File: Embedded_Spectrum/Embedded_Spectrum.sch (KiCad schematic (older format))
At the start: 20 parts, among them J1 USB_OTG, J2 AudioJack2, U1 LM1117-ADJ, U2 STM32F411RETx

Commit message: Added jack
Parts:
- removed J2: AudioJack2, symbol Connector:AudioJack2
- added C?: 100 nF, symbol Device:C
- added J2: AudioJack2_Ground, symbol Connector:AudioJack2_Ground
- added R? (x2): 10k, symbol Device:R
- added R?: 1k, symbol Device:R
- R1: value 100 -> 1000
- R2: value 220 -> 2200
- R3: value 180 -> 1800
- R4: value 820 -> 8200
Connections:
- net +3V3: now also R?.1
- net GND: now also J2.G, R?.2
- net J_IN: now reaches U2.14 (PA0)
- net J_IN: now also R?.1
- new net: C?.2, J2.S, J2.T
- new net: C?.1, R?.1, R?.2, R?.2
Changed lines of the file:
@@
 EESchema Schematic File Version 4
+LIBS:Embedded_Spectrum-cache
 EELAYER 26 0
 EELAYER END
@@
 P 4000 950
 F 0 "R1" H 4070 996 50  0000 L CNN
-F 1 "100" H 4070 905 50  0000 L CNN
+F 1 "1000" H 4070 905 50  0000 L CNN
 F 2 "" V 3930 950 50  0001 C CNN
 F 3 "~" H 4000 950 50  0001 C CNN
@@
 P 4000 1250
 F 0 "R2" H 4070 1296 50  0000 L CNN
-F 1 "220" H 4070 1205 50  0000 L CNN
+F 1 "2200" H 4070 1205 50  0000 L CNN
 F 2 "" V 3930 1250 50  0001 C CNN
 F 3 "~" H 4000 1250 50  0001 C CNN
@@
 P 4000 1550
 F 0 "R3" H 4070 1596 50  0000 L CNN
-F 1 "180" H 4070 1505 50  0000 L CNN
+F 1 "1800" H 4070 1505 50  0000 L CNN
 F 2 "" V 3930 1550 50  0001 C CNN
 F 3 "~" H 4000 1550 50  0001 C CNN
@@
 P 4000 1900
 F 0 "R4" H 4070 1946 50  0000 L CNN
-F 1 "820" H 4070 1855 50  0000 L CNN
+F 1 "8200" H 4070 1855 50  0000 L CNN
 F 2 "" V 3930 1900 50  0001 C CNN
 F 3 "~" H 4000 1900 50  0001 C CNN
@@
 $EndComp
 $Comp
-L Connector:AudioJack2 J2
-U 1 1 5C5D57A2
-P 6250 1350
-F 0 "J2" H 6280 1675 50  0000 C CNN
-F 1 "AudioJack2" H 6280 1584 50  0000 C CNN
-F 2 "" H 6250 1350 50  0001 C CNN
-F 3 "~" H 6250 1350 50  0001 C CNN
-	1    6250 1350
-	1    0    0    -1
-$EndComp
+L Connector:AudioJack2_Ground J2
+U 1 1 5C5D0CF5
+P 1500 4400
+F 0 "J2" H 1530 4725 50  0000 C CNN
+F 1 "AudioJack2_Ground" H 1530 4634 50  0000 C CNN
+F 2 "" H 1500 4400 50  0001 C CNN
+F 3 "~" H 1500 4400 50  0001 C CNN
+	1    1500 4400
+	1    0    0    -1
+$EndComp
+$Comp
+L power:GND #PWR?
+U 1 1 5C5C6E39
+P 1500 4600
+F 0 "#PWR?" H 1500 4350 50  0001 C CNN
+F 1 "GND" H 1505 4427 50  0000 C CNN
+F 2 "" H 1500 4600 50  0001 C CNN
+F 3 "" H 1500 4600 50  0001 C CNN
+	1    1500 4600
+	1    0    0    -1
+$EndComp
+Wire Wire Line
+	1700 4400 1850 4400
+Wire Wire Line
+	1700 4300 1850 4300
+Wire Wire Line
+	1850 4300 1850 4400
+Connection ~ 1850 4400
+Wire Wire Line
+	1850 4400 1950 4400
+$Comp
+L Device:C C?
+U 1 1 5C6539D7
+P 2100 4400
+F 0 "C?" V 1848 4400 50  0000 C CNN
+F 1 "100 nF" V 1939 4400 50  0000 C CNN
+F 2 "" H 2138 4250 50  0001 C CNN
+F 3 "~" H 2100 4400 50  0001 C CNN
+	1    2100 4400
+	0    1    1    0
+$EndComp
+Wire Wire Line
+	2250 4400 2350 4400
+$Comp
+L Device:R R?
+U 1 1 5C6577EA
+P 2350 4250
+F 0 "R?" H 2420 4296 50  0000 L CNN
+F 1 "10k" H 2420 4205 50  0000 L CNN
+F 2 "" V 2280 4250 50  0001 C CNN
+F 3 "~" H 2350 4250 50  0001 C CNN
+	1    2350 4250
+	1    0    0    -1
+$EndComp
+Connection ~ 2350 4400
+Wire Wire Line
+	2350 4400 2550 4400
+$Comp
+L power:+3.3V #PWR?
+U 1 1 5C657A66
+P 2350 4100
+F 0 "#PWR?" H 2350 3950 50  0001 C CNN
+F 1 "+3.3V" H 2365 4273 50  0000 C CNN
+F 2 "" H 2350 4100 50  0001 C CNN
+F 3 "" H 2350 4100 50  0001 C CNN
+	1    2350 4100
+	1    0    0    -1
+$EndComp
+$Comp
+L Device:R R?
+U 1 1 5C657C33
+P 2350 4550
+F 0 "R?" H 2420 4596 50  0000 L CNN
+F 1 "10k" H 2420 4505 50  0000 L CNN
+F 2 "" V 2280 4550 50  0001 C CNN
+F 3 "~" H 2350 4550 50  0001 C CNN
+	1    2350 4550
+	1    0    0    -1
+$EndComp
+$Comp
+L power:GND #PWR?
+U 1 1 5C6590A1
+P 2350 4700
+F 0 "#PWR?" H 2350 4450 50  0001 C CNN
+F 1 "GND" H 2355 4527 50  0000 C CNN
+F 2 "" H 2350 4700 50  0001 C CNN
+F 3 "" H 2350 4700 50  0001 C CNN
+	1    2350 4700
+	1    0    0    -1
+$EndComp
+$Comp
+L Device:R R?
+U 1 1 5C65A509
+P 2700 4400
+F 0 "R?" V 2493 4400 50  0000 C CNN
+F 1 "1k" V 2584 4400 50  0000 C CNN
+F 2 "" V 2630 4400 50  0001 C CNN
+F 3 "~" H 2700 4400 50  0001 C CNN
+	1    2700 4400
+	0    1    1    0
+$EndComp
+Wire Wire Line
+	2850 4400 2900 4400
+Text Label 2900 4400 0    50   ~ 0
+J_IN
+Text Label 5250 2950 0    50   ~ 0
+J_IN
 $EndSCHEMATC

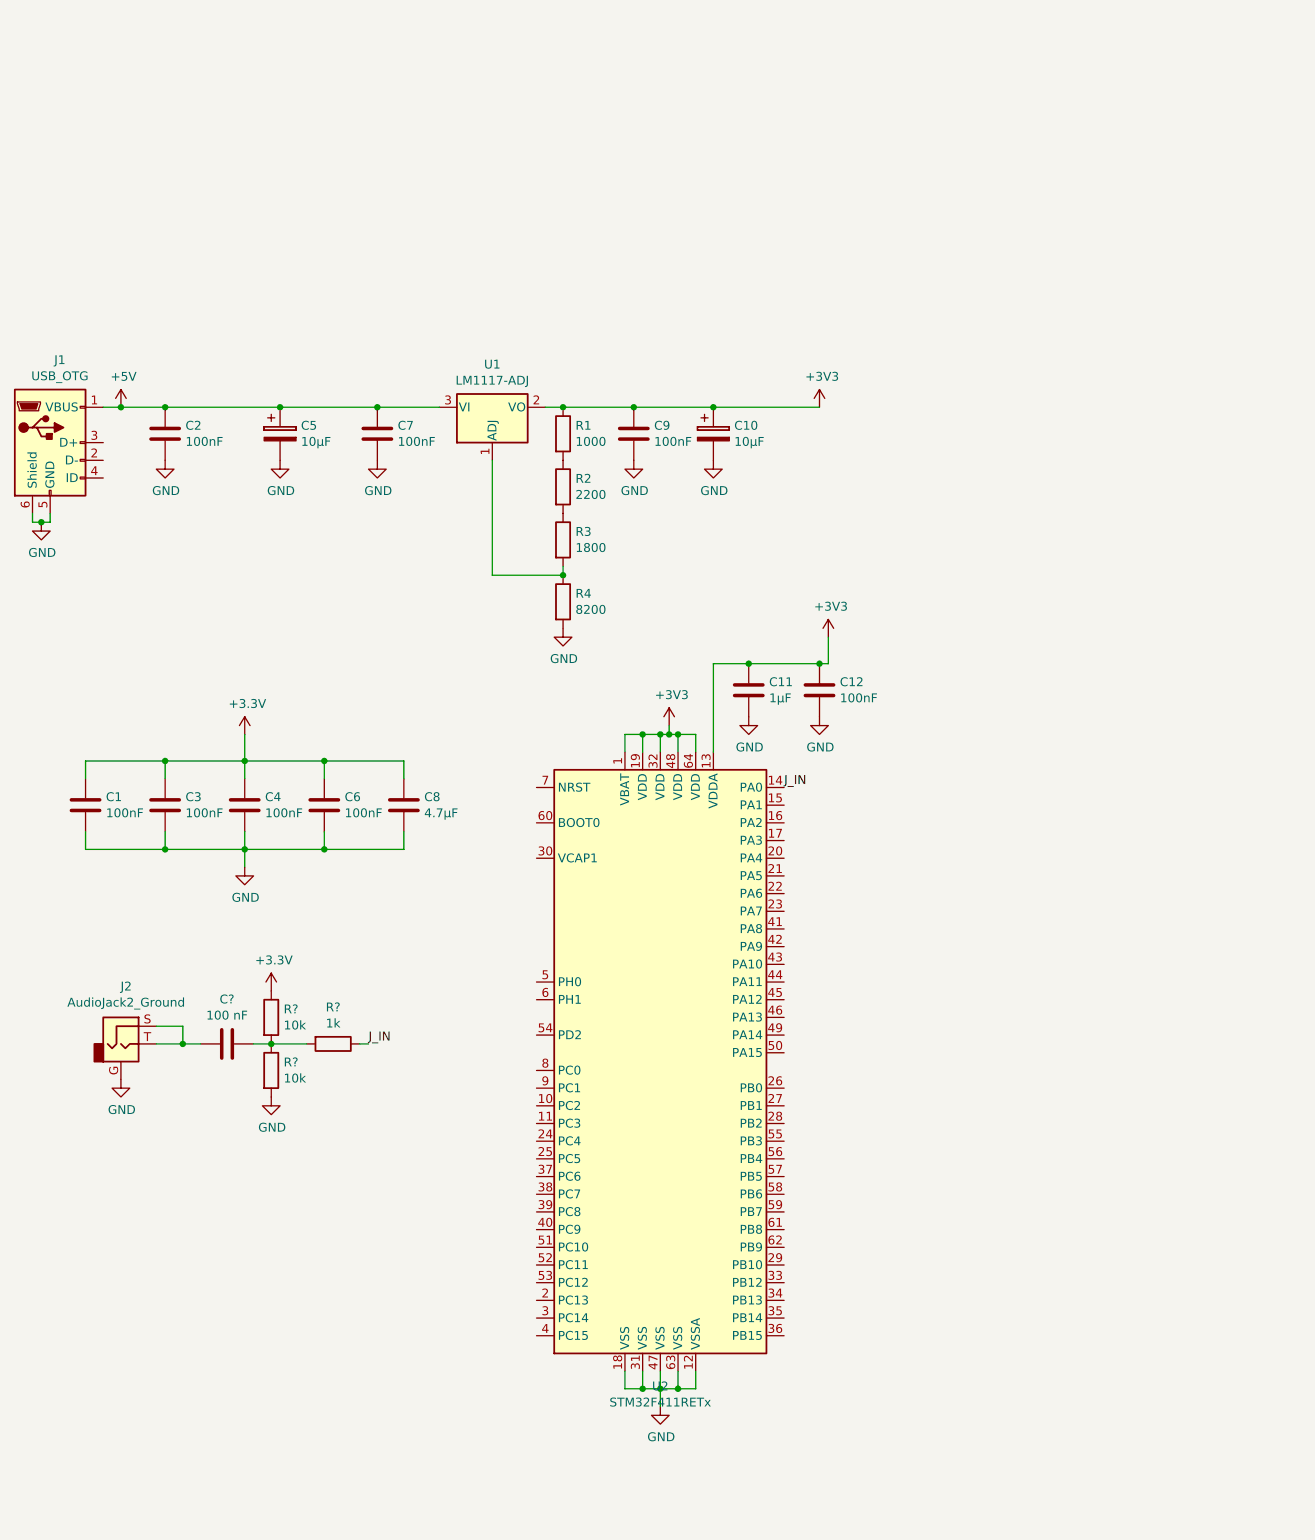
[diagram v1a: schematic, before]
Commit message: Added buttons
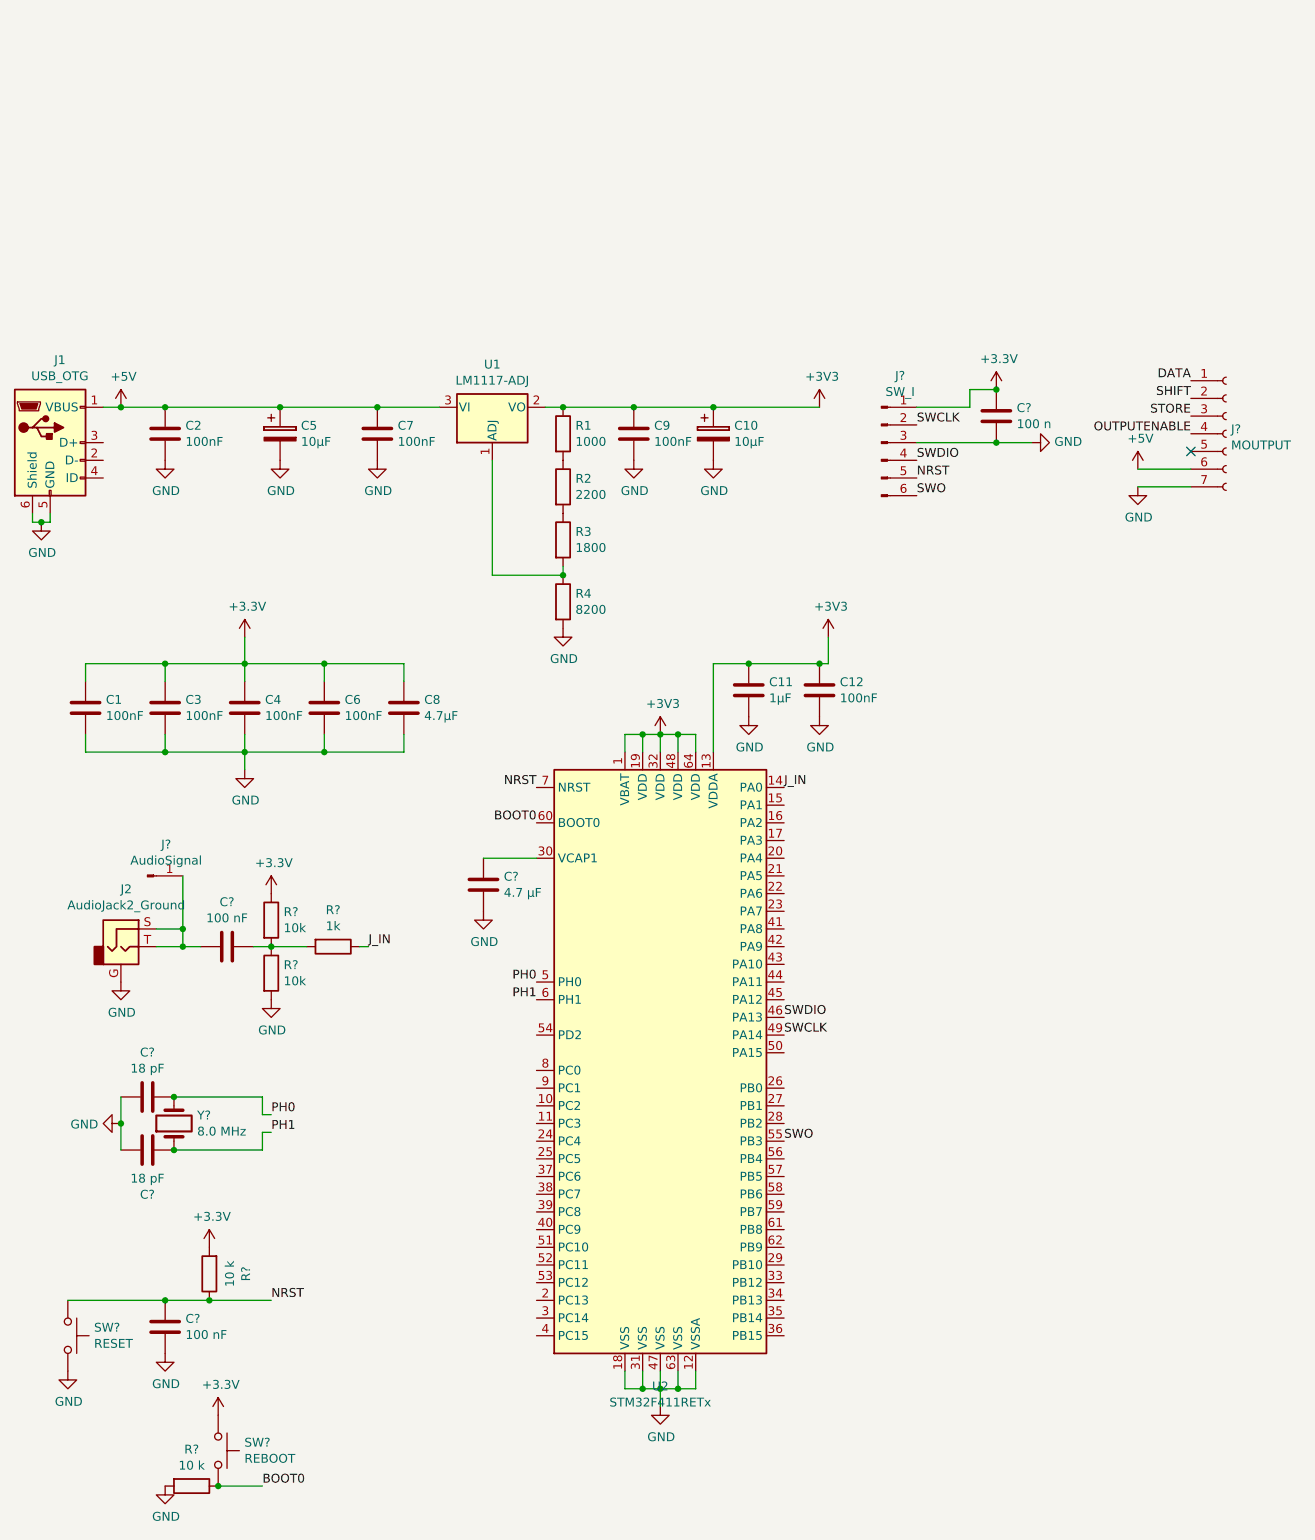
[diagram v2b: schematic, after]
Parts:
- added C? (x2): 18 pF, symbol Device:C
- added C?: 4.7 µF, symbol Device:C
- added C?: 100 n, symbol Device:C
- added C?: 100 nF, symbol Device:C
- added J?: SW_I, symbol Connector:Conn_01x06_Male
- added J?: AudioSignal, symbol Connector:Conn_01x01_Male
- added J?: MOUTPUT, symbol Connector:Conn_01x07_Female
- added R? (x2): 10 k, symbol Device:R
- added SW?: REBOOT, symbol Switch:SW_Push
- added SW?: RESET, symbol Switch:SW_Push
- added Y?: 8.0 MHz, symbol Device:Crystal
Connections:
- net +3V3: now also C?.1, J?.1 (Pin_1), R?.2, SW?.1
- net +5V: now also J?.6 (Pin_6)
- net GND: now also C?.1, C?.1, C?.2, C?.2, C?.2, J?.3 (Pin_3), J?.7 (Pin_7), R?.2, SW?.2
- net at U2.30 (VCAP1): now also C?.2
- net SWDIO: now reaches U2.46 (PA13)
- net SWDIO: now also J?.4 (Pin_4)
- net SWCLK: now reaches U2.49 (PA14)
- net SWCLK: now also J?.2 (Pin_2)
- net PH0: now reaches U2.5 (PH0)
- net PH0: now also C?.1, Y?.2
- net SWO: now reaches U2.55 (PB3)
- net SWO: now also J?.6 (Pin_6)
- net PH1: now reaches U2.6 (PH1)
- net PH1: now also C?.2, Y?.1
- net BOOT0: now reaches U2.60 (BOOT0)
- net BOOT0: now also R?.1, SW?.2
- net NRST: now reaches U2.7 (NRST)
- net NRST: now also C?.1, J?.5 (Pin_5), R?.1, SW?.1
- net at C?.2, J2.S, J2.T: now also J?.1 (Pin_1)
- new net DATA: J?.1 (Pin_1)
- new net OUTPUTENABLE: J?.4 (Pin_4)
- new net SHIFT: J?.2 (Pin_2)
- new net STORE: J?.3 (Pin_3)
- no-connect marks 0 -> 1
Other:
- moved on the sheet: C1, C3, C4, C6, C8, C?, J2, R?

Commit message: Half of the control PCB blueprints added
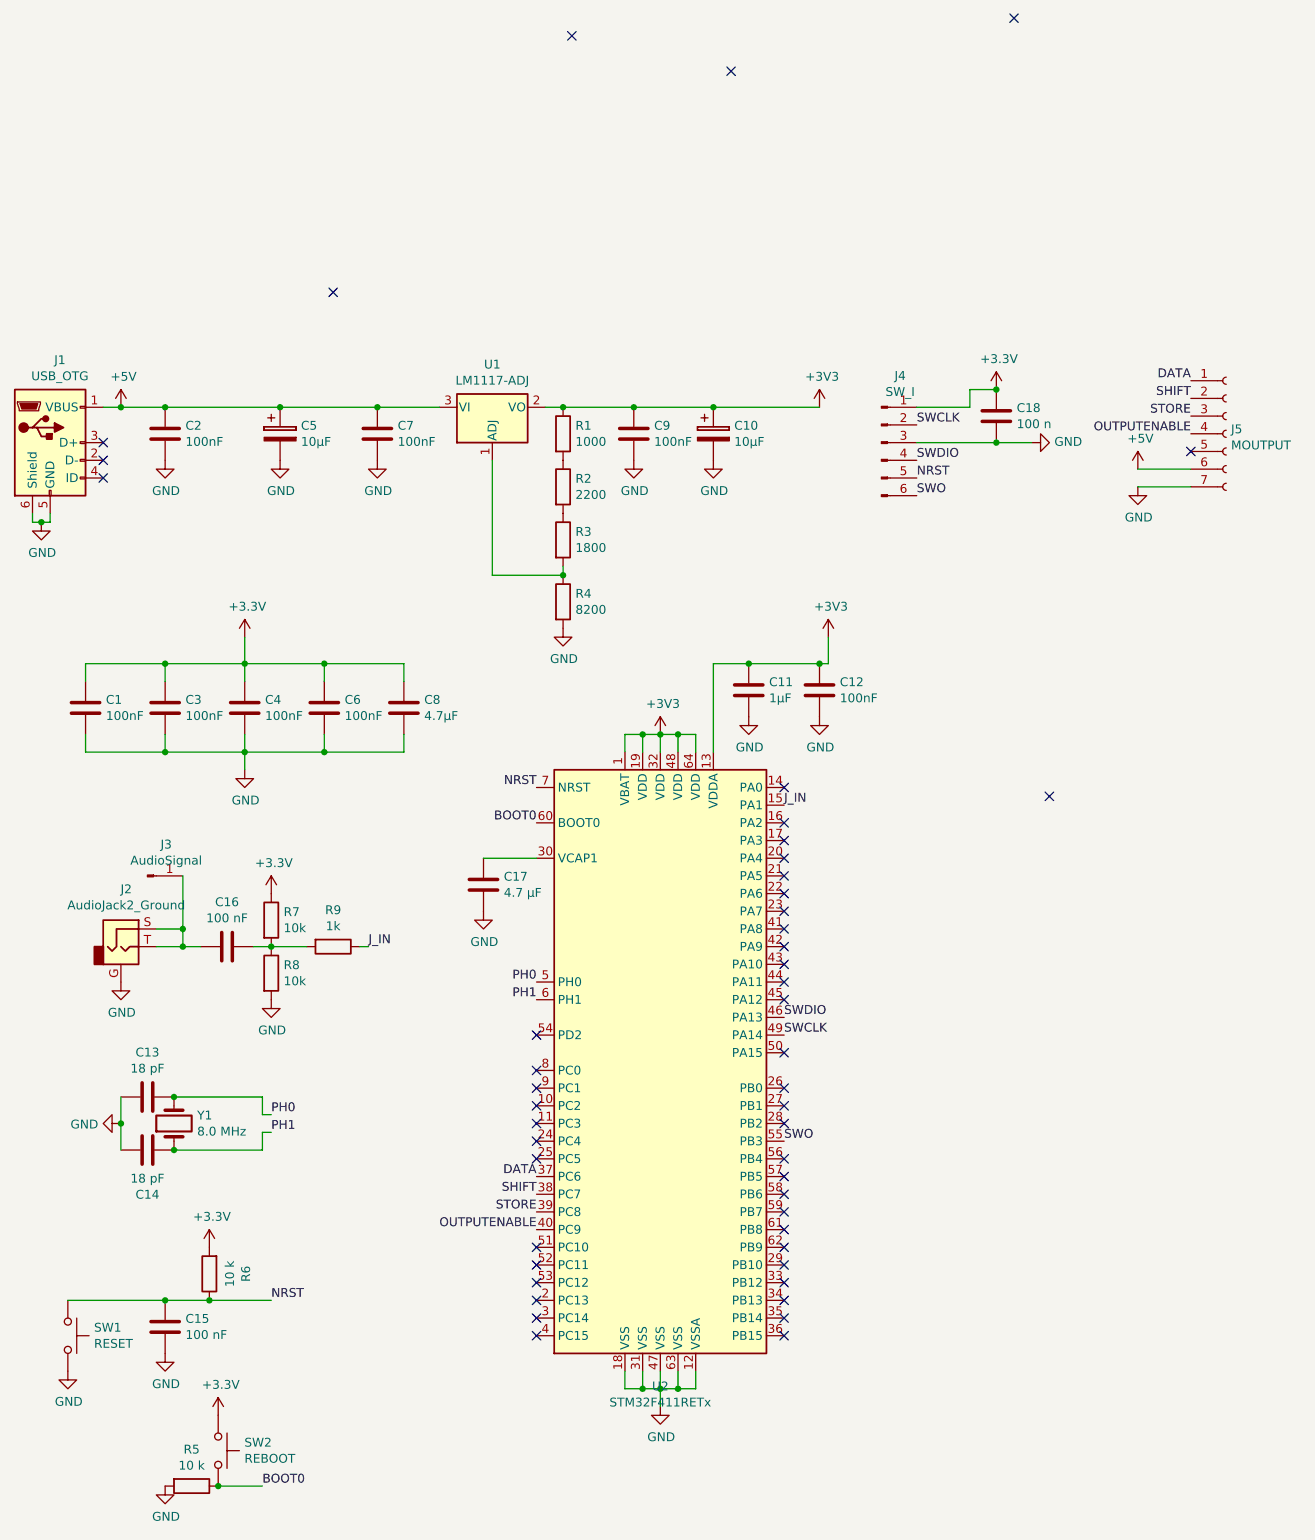
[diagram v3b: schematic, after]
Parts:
- C1, C11, C12, C2, C3, C4, C6, C7, C8, C9: footprint (none) -> Capacitor_SMD:C_0805_2012Metric_Pad1.15x1.40mm_HandSolder
- C10, C5: footprint (none) -> Capacitor_SMD:CP_Elec_4x5.4
- C13, C14, C15, C16, C17, C18: renamed from C?; footprint (none) -> Capacitor_SMD:C_0805_2012Metric_Pad1.15x1.40mm_HandSolder
- J2: footprint (none) -> Our_Components:PJ-211_Phone-Jack
- R1, R2, R3, R4: footprint (none) -> Resistor_SMD:R_0805_2012Metric_Pad1.15x1.40mm_HandSolder
- R5, R6, R7, R8, R9: renamed from R?; footprint (none) -> Resistor_SMD:R_0805_2012Metric_Pad1.15x1.40mm_HandSolder
- Y1: renamed from Y?; footprint (none) -> Crystal:Crystal_SMD_HC49-SD_HandSoldering
- gave numbers to parts that had none: 5
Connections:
- net DATA: now also U2.37 (PC6)
- net J_IN: now also U2.15 (PA1); no longer U2.14 (PA0)
- net OUTPUTENABLE: now also U2.40 (PC9)
- net SHIFT: now also U2.38 (PC7)
- net STORE: now also U2.39 (PC8)
- no-connect marks 1 -> 49
